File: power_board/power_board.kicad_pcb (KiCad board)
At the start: 4 copper layers, 87 x 57 mm, 14 parts, among them J1 AC2, J2 AC3, J3 AC1, J4 VCCB, J5 VCCA

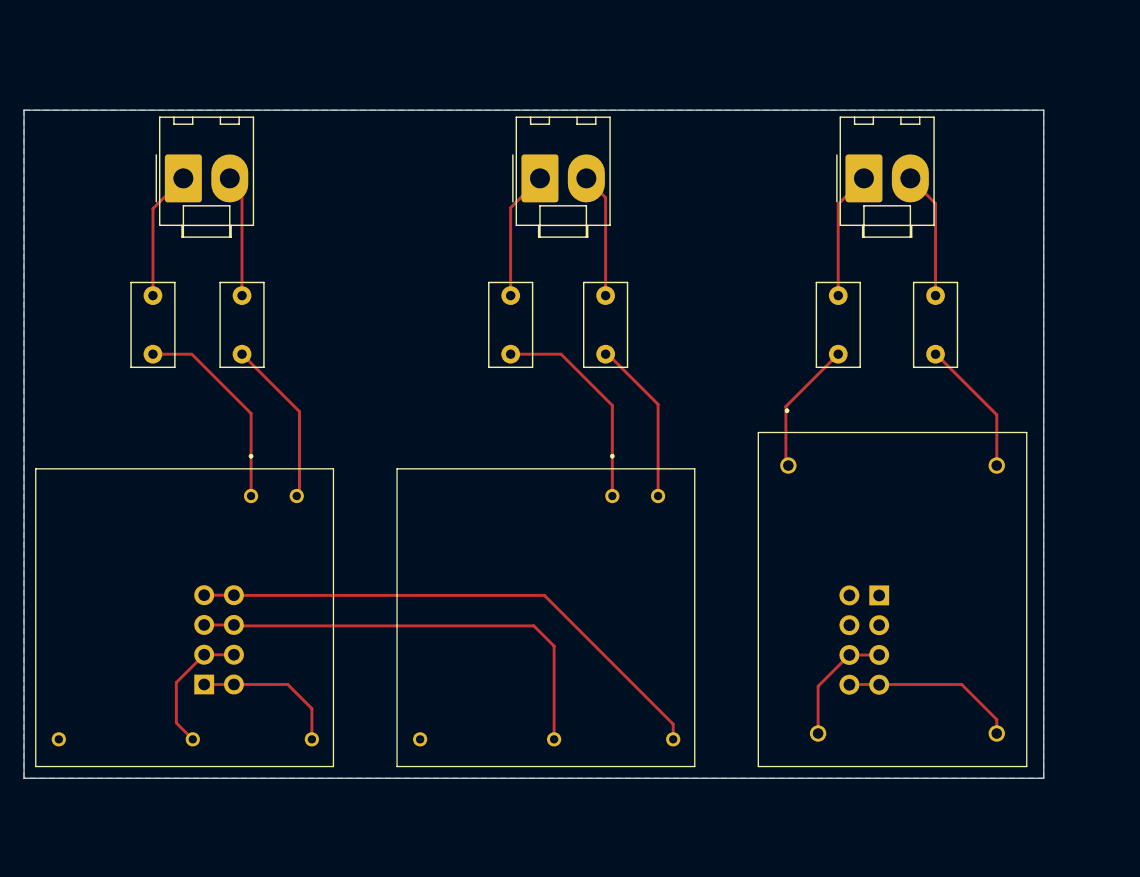
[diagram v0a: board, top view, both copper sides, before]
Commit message: redesigned the power loop
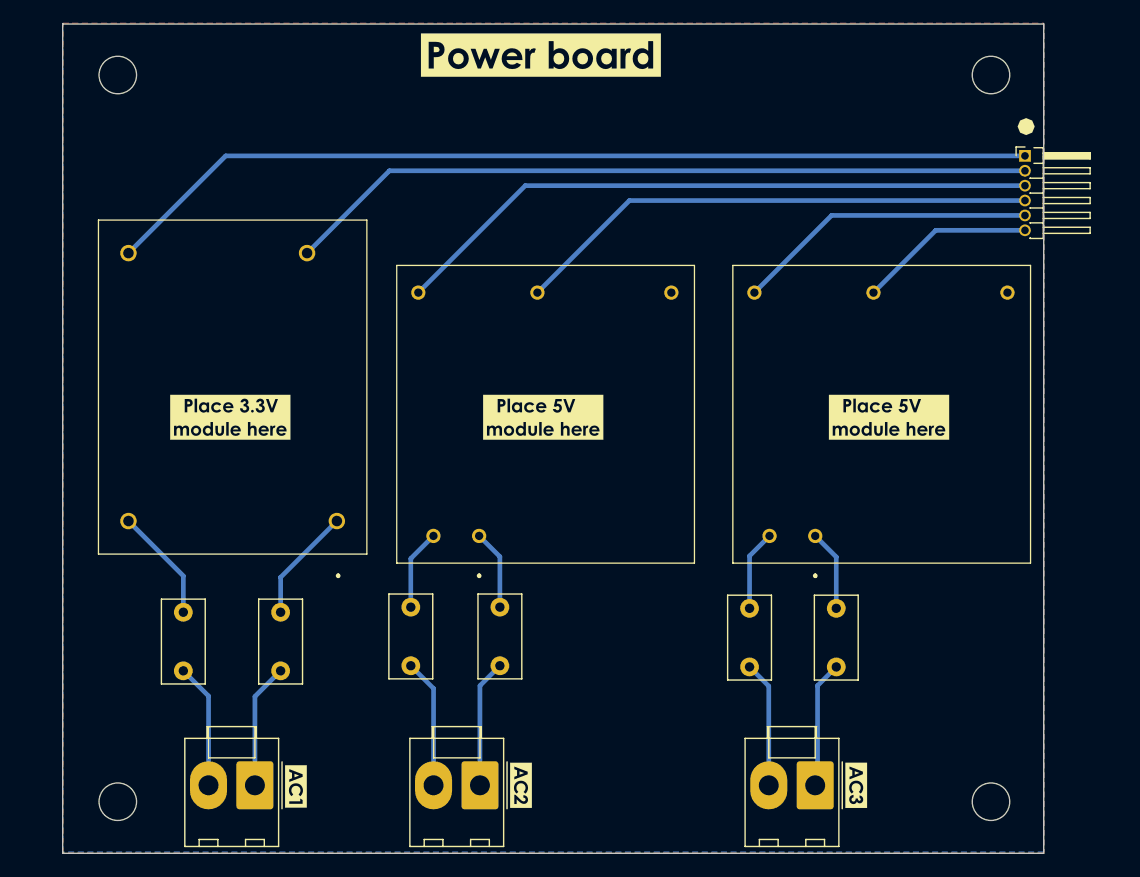
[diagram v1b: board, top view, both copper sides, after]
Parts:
- removed J5: VCCA, Connector_PinHeader_2.54mm:PinHeader_2x04_P2.54mm_Vertical
- added H1: MountingHole, MountingHole:MountingHole_3.2mm_M3, F.Cu at (101.8, 61.8)
- added H2: MountingHole, MountingHole:MountingHole_3.2mm_M3, F.Cu at (176.3, 123.8)
- added H3: MountingHole, MountingHole:MountingHole_3.2mm_M3, F.Cu at (176.3, 61.8)
- added H4: MountingHole, MountingHole:MountingHole_3.2mm_M3, F.Cu at (101.8, 123.8)
- added kibuzzard-63EE9CC7: G***, kibuzzard-63EE9CC7, F.Cu at (111.4, 91.0)
- added kibuzzard-63EE9CEB: G***, kibuzzard-63EE9CEB, F.Cu at (138.1, 91.0)
- added kibuzzard-63EE9CF3: G***, kibuzzard-63EE9CF3, F.Cu at (167.6, 91.0)
- added kibuzzard-63EE9D9B: G***, kibuzzard-63EE9D9B, F.Cu at (179.3, 66.2)
- added kibuzzard-63EEA033: G***, kibuzzard-63EEA033, F.Cu at (117.0, 122.5)
- added kibuzzard-63EEA069: G***, kibuzzard-63EEA069, F.Cu at (136.2, 122.4)
- added kibuzzard-63EEA072: G***, kibuzzard-63EEA072, F.Cu at (164.8, 122.4)
- added kibuzzard-63EEA0F8: G***, kibuzzard-63EEA0F8, F.Cu at (137.9, 60.1)
- J4: value VCCB -> Conn_01x06_Male; footprint Connector_PinHeader_2.54mm:PinHeader_2x04_P2.54mm_Vertical -> Connector_PinHeader_1.27mm:PinHeader_1x06_P1.27mm_Horizontal; moved to F.Cu
- moved J4 83.3 mm to (179.2, 68.7)
- moved J3 73.4 mm to (113.5, 122.4), turned to 180 degrees
- moved L1 71.7 mm to (107.4, 112.6), turned to 90 degrees
- moved J1 57.6 mm to (132.7, 122.4), turned to 180 degrees
- moved L2 57.3 mm to (115.7, 112.6), turned to 90 degrees
- moved J2 56.9 mm to (161.3, 122.4), turned to 180 degrees
- moved L4 43.3 mm to (134.4, 112.2), turned to 90 degrees
- moved L6 42.1 mm to (163.1, 112.3), turned to 90 degrees
- moved PS1 38.8 mm to (120.5, 99.9), turned to 90 degrees
- moved L3 34.7 mm to (126.8, 112.2), turned to 90 degrees
- moved L5 34.0 mm to (155.7, 112.3), turned to 90 degrees
- moved PS2 19.8 mm to (132.6, 101.1), turned to 90 degrees
- moved PS3 17.6 mm to (161.3, 101.1), turned to 90 degrees
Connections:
- J4 pad 2: Net-(J4-Pad1) -> Net-(J4-Pad2)
- J4 pad 4: Net-(J4-Pad3) -> Net-(J4-Pad4)
- J4 pad 6: Net-(J4-Pad5) -> Net-(J4-Pad6)
- PS1 pad 2: Net-(J5-Pad5) -> Net-(J4-Pad2)
- PS1 pad 3: Net-(J5-Pad7) -> Net-(J4-Pad1)
- PS2 pad 4: Net-(J4-Pad3) -> Net-(J4-Pad4)
- PS2 pad 5: Net-(J4-Pad1) -> Net-(J4-Pad3)
- PS3 pad 4: Net-(J4-Pad5) -> Net-(J4-Pad6)
- PS3 pad 5: Net-(J4-Pad7) -> Net-(J4-Pad5)
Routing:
- net Net-(J4-Pad1): track 12.7 -> 79.9 mm
- net Net-(J4-Pad2): track 0.00 -> 64.2 mm
- net Net-(J4-Pad7): track 45.9 -> 0.00 mm
- net Net-(J4-Pad4): track 0.00 -> 44.9 mm
- net Net-(J4-Pad3): track 11.3 -> 55.5 mm
- net Net-(J4-Pad6): track 0.00 -> 15.1 mm
- net Net-(J5-Pad7): track 15.0 -> 0.00 mm
- net Net-(J4-Pad5): track 38.6 -> 25.8 mm
- net Net-(L6-Pad2): track 18.2 -> 6.92 mm
- net Net-(L4-Pad2): track 17.5 -> 6.81 mm
- net Net-(J5-Pad5): track 10.3 -> 0.00 mm
- net Net-(L3-Pad2): track 14.2 -> 6.87 mm
- net Net-(L5-Pad2): track 14.1 -> 6.98 mm
- net Net-(L1-Pad2): track 11.7 -> 9.72 mm
- net Net-(L2-Pad2): track 11.4 -> 9.77 mm
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- added copper zone on F.Cu, net (none)
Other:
- board size 87 x 57 mm -> 83.7 x 70.8 mm
- copper layers 4 -> 2

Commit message: Updated final design
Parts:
- J4: value Conn_01x06_Male -> Conn_02x05_Odd_Even; footprint Connector_PinHeader_1.27mm:PinHeader_1x06_P1.27mm_Horizontal -> 61201021621:SHDR10W64P254_2X5_2036X885X925P
- moved kibuzzard-63EE9D9B 51.6 mm to (128.2, 59.5)
- moved J4 44.8 mm to (134.6, 63.7)
- moved kibuzzard-63EEA0F8 9.76 mm to (139.9, 69.7)
- moved H3 0.82 mm to (175.8, 62.5)
- moved H2 0.78 mm to (175.8, 123.2)
- moved H1 0.72 mm to (102.1, 62.5)
- moved H4 0.67 mm to (102.1, 123.2)
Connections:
- PS1 pad 2: Net-(J4-Pad2) -> Net-(J4-Pad1)
- PS1 pad 3: Net-(J4-Pad1) -> Net-(J4-Pad2)
- PS2 pad 4: Net-(J4-Pad4) -> Net-(J4-Pad3)
- PS2 pad 5: Net-(J4-Pad3) -> Net-(J4-Pad4)
- PS3 pad 4: Net-(J4-Pad6) -> Net-(J4-Pad5)
- PS3 pad 5: Net-(J4-Pad5) -> Net-(J4-Pad6)
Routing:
- net Net-(J4-Pad1): track 79.9 -> 26.6 mm
- net Net-(J4-Pad3): track 55.5 -> 16.8 mm
- net Net-(J4-Pad2): track 64.2 -> 38.5 mm
- net Net-(J4-Pad4): track 44.9 -> 26.6 mm
- net Net-(J4-Pad6): track 15.1 -> 31.1 mm
- net Net-(J4-Pad5): track 25.8 -> 33.5 mm
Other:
- outline, holes or cut-outs redrawn

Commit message: Final design
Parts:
- J4: value Conn_02x05_Odd_Even -> Conn_02x03_Odd_Even; footprint 61201021621:SHDR10W64P254_2X5_2036X885X925P -> Connector_PinHeader_2.54mm:PinHeader_2x03_P2.54mm_Horizontal
- moved kibuzzard-63EE9D9B 51.8 mm to (179.5, 66.5)
- moved J4 40.1 mm to (174.3, 69.4)
- moved kibuzzard-63EEA0F8 4.90 mm to (139.8, 64.8)
- moved L2 1.12 mm to (114.6, 112.9)
- moved L6 0.78 mm to (162.6, 112.9)
- moved L4 0.76 mm to (134.1, 112.9)
- moved L3 0.76 mm to (127.1, 112.9)
- moved L5 0.61 mm to (155.6, 112.9)
- moved L1 0.34 mm to (107.6, 112.9)
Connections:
- J4 pad 1: Net-(J4-Pad1) -> Net-(J4-Pin_1)
- J4 pad 2: Net-(J4-Pad2) -> Net-(J4-Pin_2)
- J4 pad 3: Net-(J4-Pad3) -> Net-(J4-Pin_3)
- J4 pad 4: Net-(J4-Pad4) -> Net-(J4-Pin_4)
- J4 pad 5: Net-(J4-Pad5) -> Net-(J4-Pin_5)
- J4 pad 6: Net-(J4-Pad6) -> Net-(J4-Pin_6)
- PS1 pad 2: Net-(J4-Pad1) -> Net-(J4-Pin_2)
- PS1 pad 3: Net-(J4-Pad2) -> Net-(J4-Pin_1)
- PS2 pad 4: Net-(J4-Pad3) -> Net-(J4-Pin_4)
- PS2 pad 5: Net-(J4-Pad4) -> Net-(J4-Pin_3)
- PS3 pad 4: Net-(J4-Pad5) -> Net-(J4-Pin_6)
- PS3 pad 5: Net-(J4-Pad6) -> Net-(J4-Pin_5)
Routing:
- net Net-(J4-Pin_1): track 0.00 -> 74.7 mm
- net Net-(J4-Pin_2): track 0.00 -> 62.0 mm
- net Net-(J4-Pin_3): track 0.00 -> 50.3 mm
- net Net-(J4-Pin_4): track 0.00 -> 42.7 mm
- net Net-(J4-Pad2): track 38.5 -> 0.00 mm
- net Net-(J4-Pad5): track 33.5 -> 0.00 mm
- net Net-(J4-Pad6): track 31.1 -> 0.00 mm
- net Net-(J4-Pad1): track 26.6 -> 0.00 mm
- net Net-(J4-Pad4): track 26.6 -> 0.00 mm
- net Net-(J4-Pin_5): track 0.00 -> 20.6 mm
- net Net-(J4-Pad3): track 16.8 -> 0.00 mm
- net Net-(J4-Pin_6): track 0.00 -> 14.2 mm
- net Net-(J3-Pin_1): track 10.9 -> 9.96 mm
- net Net-(J1-Pin_1): track 10.9 -> 10.1 mm
- net Net-(J1-Pin_2): track 11.0 -> 10.2 mm
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
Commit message: added logo
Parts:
- removed kibuzzard-63EEA0F8: G***, kibuzzard-63EEA0F8
- added G***: LOGO, logo:IITDh logo, F.Cu at (148.7, 61.1)
- added G***: LOGO, logo:IITDh logo, F.Cu at (132.5, 61.1)
- added kibuzzard-640AA3C8: G***, kibuzzard-640AA3C8, F.Cu at (140.6, 61.1)
- added kibuzzard-640AA5A5: G***, kibuzzard-640AA5A5, F.Cu at (140.6, 63.3)

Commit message: changed cap values
PWM RC filter caps changed from 100nF to 0.1nF because of limitations
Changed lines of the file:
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@@
   )
   (paper "A4")
+  (title_block
+    (comment 4 "AISLER Project ID: LAREALUL")
+  )
   (layers
     (0 "F.Cu" mixed)
@@
     (fp_line (start 5.87 3.895) (end 3.965 3.895)
       (stroke (width 0.1) (type solid)) (layer "F.Fab"))
-    (pad "1" thru_hole roundrect (at 0 0 180) (size 3.16 4.1) (drill 1.7) (layers "*.Cu" "*.Mask") (roundrect_rratio 0.079114)
+    (pad "1" thru_hole roundrect (at 0 0 180) (size 3.16 4.1) (drill 1.7) (layers "*.Cu" "*.Mask") (roundrect_rratio 0.07911392405)
       (net 1 "Net-(J1-Pin_1)") (pinfunction "Pin_1") (pintype "passive"))
     (pad "2" thru_hole oval (at 3.96 0 180) (size 3.16 4.1) (drill 1.7) (layers "*.Cu" "*.Mask")
@@
     (attr board_only exclude_from_pos_files exclude_from_bom)
     (fp_text reference "kibuzzard-640AA5A5" (at 0 -3.974042) (layer "F.SilkS") hide
-        (effects (font (size 0 0)))
+        (effects (font (size 0 0) (thickness 0.15)))
     )
     (fp_text value "G***" (at 0 3.974042) (layer "F.SilkS") hide
-        (effects (font (size 0 0)))
+        (effects (font (size 0 0) (thickness 0.15)))
     )
     (fp_poly
@@
     (fp_line (start 5.87 3.895) (end 3.965 3.895)
       (stroke (width 0.1) (type solid)) (layer "F.Fab"))
-    (pad "1" thru_hole roundrect (at 0 0 180) (size 3.16 4.1) (drill 1.7) (layers "*.Cu" "*.Mask") (roundrect_rratio 0.079114)
+    (pad "1" thru_hole roundrect (at 0 0 180) (size 3.16 4.1) (drill 1.7) (layers "*.Cu" "*.Mask") (roundrect_rratio 0.07911392405)
       (net 3 "Net-(J2-Pin_1)") (pinfunction "Pin_1") (pintype "passive"))
     (pad "2" thru_hole oval (at 3.96 0 180) (size 3.16 4.1) (drill 1.7) (layers "*.Cu" "*.Mask")
@@
     (fp_line (start 5.87 3.895) (end 3.965 3.895)
       (stroke (width 0.1) (type solid)) (layer "F.Fab"))
-    (pad "1" thru_hole roundrect (at 0 0 180) (size 3.16 4.1) (drill 1.7) (layers "*.Cu" "*.Mask") (roundrect_rratio 0.079114)
+    (pad "1" thru_hole roundrect (at 0 0 180) (size 3.16 4.1) (drill 1.7) (layers "*.Cu" "*.Mask") (roundrect_rratio 0.07911392405)
       (net 5 "Net-(J3-Pin_1)") (pinfunction "Pin_1") (pintype "passive"))
     (pad "2" thru_hole oval (at 3.96 0 180) (size 3.16 4.1) (drill 1.7) (layers "*.Cu" "*.Mask")
